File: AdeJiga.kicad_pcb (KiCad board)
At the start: 2 copper layers, 82 x 78 mm, 40 parts, among them J1 Screw_Terminal_01x03, J10 Conn_01x02_Pin, J11 Conn_01x02_Pin, J12 Screw_Terminal_01x03, J2 Screw_Terminal_01x02, J3 Screw_Terminal_01x03, J4 Conn_01x05_Pin, J5 Conn_01x02_Pin, J6 Conn_01x03_Pin, J7 Conn_01x02_Pin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

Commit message: Versão 3 consolidada, placa fabricada
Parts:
- added C3: 220uF, Capacitor_THT:CP_Radial_D6.3mm_P2.50mm, F.Cu at (174.0, 166.5)
- added D1: 1N4007, Diode_THT:D_DO-41_SOD81_P10.16mm_Horizontal, F.Cu at (137.5, 112.4)
- added D2: 1N4007, Diode_THT:D_DO-41_SOD81_P10.16mm_Horizontal, F.Cu at (137.5, 129.3)
- added D3: LED, LED_THT:LED_D5.0mm_Clear, F.Cu at (152.0, 115.2)
- added D4: 1N4007, Diode_THT:D_DO-41_SOD81_P10.16mm_Horizontal, F.Cu at (124.8, 166.2)
- added D5: LED, LED_THT:LED_D5.0mm_Clear, F.Cu at (152.1, 132.2)
- added D6: 1N4007, Diode_THT:D_DO-41_SOD81_P10.16mm_Horizontal, F.Cu at (137.5, 145.8)
- added D7: LED, LED_THT:LED_D5.0mm_Clear, F.Cu at (151.8, 151.8)
- added H1: MountingHole, MountingHole:MountingHole_3.2mm_M3_DIN965, F.Cu at (112.0, 175.2)
- added H2: MountingHole, MountingHole:MountingHole_3.2mm_M3_DIN965, F.Cu at (181.0, 175.7)
- added H3: MountingHole, MountingHole:MountingHole_3.2mm_M3_DIN965, F.Cu at (112.0, 104.7)
- added H4: MountingHole, MountingHole:MountingHole_3.2mm_M3_DIN965, F.Cu at (181.0, 104.7)
- added J1: Screw_Terminal_01x03, TerminalBlock_MetzConnect:TerminalBlock_MetzConnect_Type011_RT05503HBWC_1x03_P5.00mm_Horizontal, F.Cu at (115.3, 122.0)
- added J10: Conn_01x02_Pin, Connector_PinHeader_2.54mm:PinHeader_1x02_P2.54mm_Vertical, F.Cu at (171.8, 176.0)
- added J11: Conn_01x02_Pin, Connector_PinHeader_2.54mm:PinHeader_1x02_P2.54mm_Vertical, F.Cu at (118.5, 162.7)
- added J12: Screw_Terminal_01x03, TerminalBlock_MetzConnect:TerminalBlock_MetzConnect_Type011_RT05503HBWC_1x03_P5.00mm_Horizontal, F.Cu at (115.2, 156.0)
- added J2: Screw_Terminal_01x02, TerminalBlock_MetzConnect:TerminalBlock_MetzConnect_Type011_RT05502HBWC_1x02_P5.00mm_Horizontal, F.Cu at (118.8, 175.0)
- added J3: Screw_Terminal_01x03, TerminalBlock_MetzConnect:TerminalBlock_MetzConnect_Type011_RT05503HBWC_1x03_P5.00mm_Horizontal, F.Cu at (115.3, 139.0)
- added J4: Conn_01x05_Pin, Connector_PinSocket_2.54mm:PinSocket_1x05_P2.54mm_Vertical, F.Cu at (151.7, 103.0)
- added J5: Conn_01x02_Pin, Connector_PinHeader_2.54mm:PinHeader_1x02_P2.54mm_Vertical, F.Cu at (158.8, 130.7)
- added J6: Conn_01x03_Pin, Connector_PinHeader_2.54mm:PinHeader_1x03_P2.54mm_Vertical, F.Cu at (174.2, 124.7)
- added J7: Conn_01x02_Pin, Connector_PinHeader_2.54mm:PinHeader_1x02_P2.54mm_Vertical, F.Cu at (175.5, 176.0)
- added J8: Conn_01x03_Pin, Connector_PinHeader_2.54mm:PinHeader_1x03_P2.54mm_Vertical, F.Cu at (171.7, 103.0)
- added J9: Conn_01x04_Pin, Connector_PinHeader_2.54mm:PinHeader_1x04_P2.54mm_Vertical, F.Cu at (162.9, 103.0)
- added K1: JJM1C_relay, Benzlab:JJM1C_relay, F.Cu at (128.0, 117.0)
- added K2: JJM1C_relay, Benzlab:JJM1C_relay, F.Cu at (127.9, 134.0)
- added K3: JJM1C_relay, Benzlab:JJM1C_relay, F.Cu at (128.0, 149.7)
- added M1: DC-DC-STEP-DOWN-LM2596, Benzlab:DC-DC-STEP-DOWN-LM2596, F.Cu at (148.2, 168.2)
- added Q1: TIP127, Package_TO_SOT_THT:TO-220-3_Vertical, F.Cu at (145.3, 113.7)
- added Q2: TIP127, Package_TO_SOT_THT:TO-220-3_Vertical, F.Cu at (145.0, 147.5)
- added Q3: TIP127, Package_TO_SOT_THT:TO-220-3_Vertical, F.Cu at (145.1, 130.6)
- added R1: 3.3k, Resistor_THT:R_Axial_DIN0207_L6.3mm_D2.5mm_P10.16mm_Horizontal, F.Cu at (142.0, 122.2)
- added R2: 220, Resistor_THT:R_Axial_DIN0207_L6.3mm_D2.5mm_P10.16mm_Horizontal, F.Cu at (154.8, 123.2)
- added R3: 3.3k, Resistor_THT:R_Axial_DIN0207_L6.3mm_D2.5mm_P10.16mm_Horizontal, F.Cu at (141.8, 139.2)
- added R4: 220, Resistor_THT:R_Axial_DIN0207_L6.3mm_D2.5mm_P10.16mm_Horizontal, F.Cu at (155.1, 140.0)
- added R5: 0, Resistor_THT:R_Axial_DIN0204_L3.6mm_D1.6mm_P5.08mm_Vertical, F.Cu at (178.0, 121.7)
- added R7: 220, Resistor_THT:R_Axial_DIN0207_L6.3mm_D2.5mm_P10.16mm_Horizontal, F.Cu at (145.0, 157.0)
- added R8: 3.3k, Resistor_THT:R_Axial_DIN0207_L6.3mm_D2.5mm_P10.16mm_Horizontal, F.Cu at (141.8, 156.1)
- added U2: ESP32-WROOM-32, RF_Module:ESP32-WROOM-32, B.Cu at (169.3, 142.3)
- added U4: AMS1117, Package_TO_SOT_SMD:SOT-223-3_TabPin2, B.Cu at (174.2, 158.5)
- moved H1 77.1 mm to (112.0, 92.8), turned to -90 degrees
- moved H3 73.9 mm to (112.0, 22.2), turned to -90 degrees
- moved J2 70.3 mm to (118.8, 92.5), turned to 0 degrees
- moved H2 65.7 mm to (181.0, 93.2), turned to -90 degrees
- moved H4 64.3 mm to (181.0, 22.2), turned to -90 degrees
- moved J7 62.2 mm to (175.5, 93.5), turned to 180 degrees
- moved J10 59.6 mm to (171.8, 93.5), turned to 180 degrees
- moved J11 59.1 mm to (118.5, 80.2), turned to 90 degrees
- moved J12 58.2 mm to (115.2, 73.5), turned to 90 degrees
- moved J8 57.6 mm to (171.7, 20.5), turned to -90 degrees
- moved J1 57.5 mm to (115.3, 39.5), turned to 90 degrees
- moved D4 55.4 mm to (124.8, 83.8), turned to 180 degrees
- moved J9 52.8 mm to (162.9, 20.5), turned to -90 degrees
- moved J3 52.5 mm to (115.3, 56.5), turned to 90 degrees
- moved J4 50.7 mm to (151.7, 20.5), turned to -90 degrees
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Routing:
- net GND: track 283.2 -> 554.3 mm
- net +5V: track 202.5 -> 416.6 mm
- net GPIOA: track 37.7 -> 74.2 mm
- net GPIOB: track 37.1 -> 73.1 mm
- net GPIOC: track 36.9 -> 72.1 mm
- net GPIOD: track 35.6 -> 70.1 mm
- net GPIOE: track 35.1 -> 69.1 mm
- net GPIOF: track 34.6 -> 68.0 mm
- net GPIOG: track 34.1 -> 67.3 mm
- net GPIOH: track 33.0 -> 65.0 mm
- net REL3: track 29.2 -> 58.4 mm
- net +3.3V: track 25.0 -> 50.0 mm
- net REL2: track 23.2 -> 46.3 mm
- net REL1: track 25.6 -> 47.4 mm
- net Net-(J12-Pin_2): track 20.2 -> 40.5 mm
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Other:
- board size 82 x 78 mm -> 78 x 162.2 mm
- board text removed: "-"
- board text removed: "3V3"
- board text removed: "5V"
- board text removed: "A"
- board text removed: "B"
- board text removed: "C"
- board text removed: "D"
- board text removed: "E"
- board text removed: "F"
- board text removed: "G"
- board text removed: "H"
- board text removed: "NA"
- board text removed: "NF"

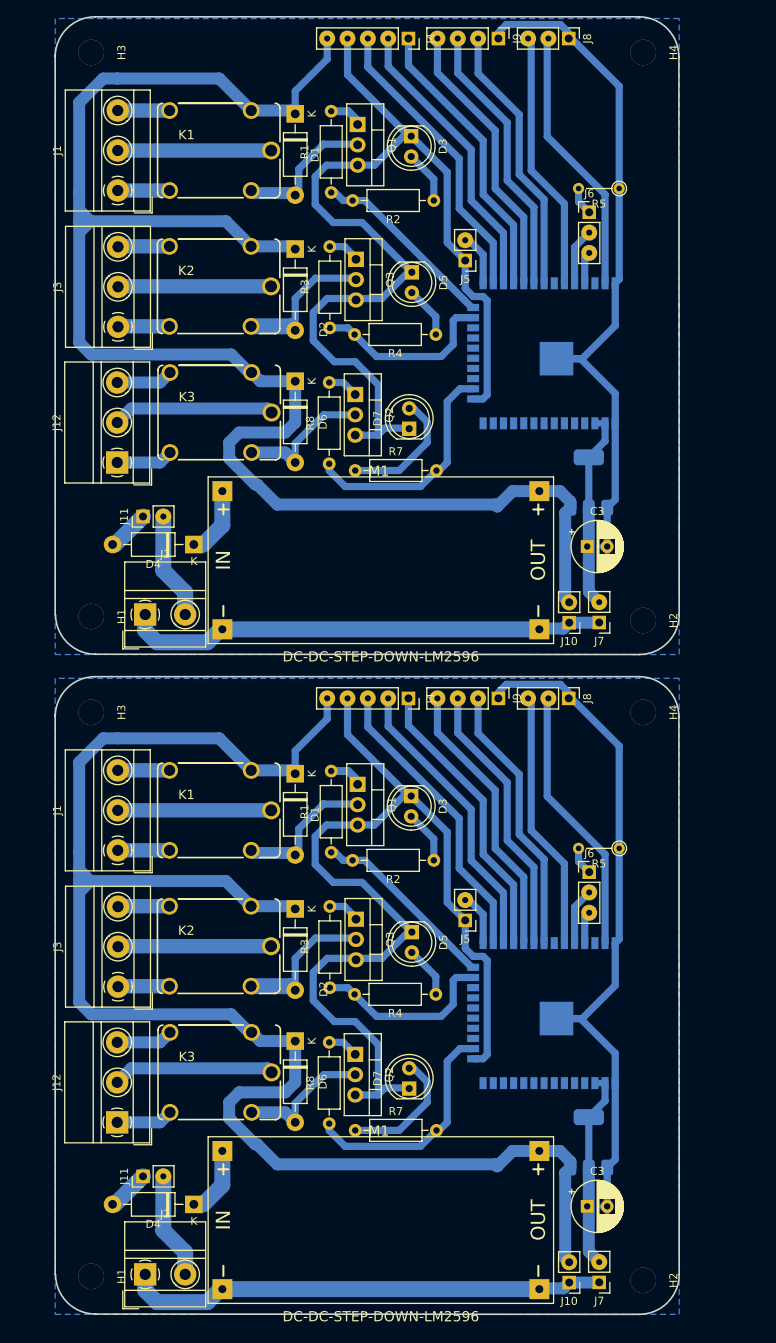
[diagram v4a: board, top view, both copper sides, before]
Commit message: modificações no layout da placa e modelo 3d
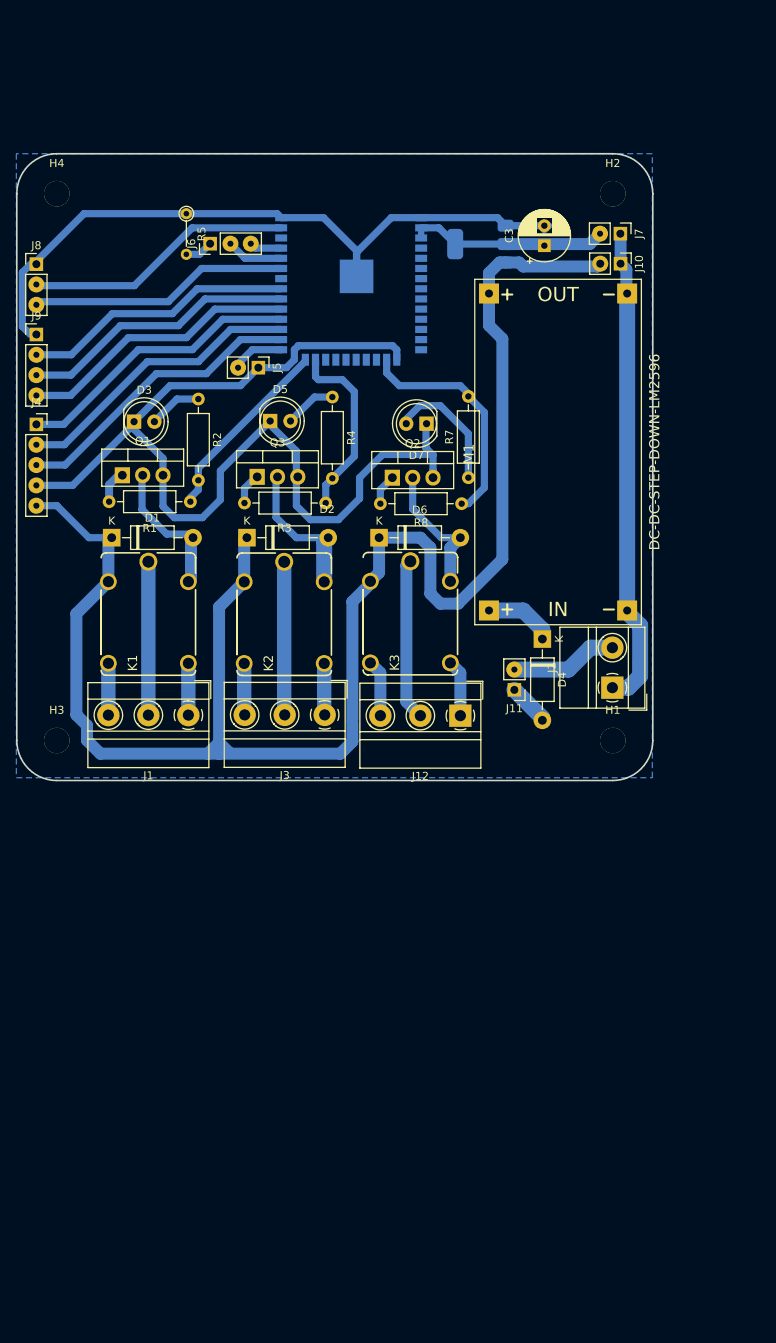
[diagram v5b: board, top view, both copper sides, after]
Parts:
- removed the C3 at (174.0, 166.5)
- removed the D1 at (137.5, 112.4)
- removed the D2 at (137.5, 129.3)
- removed the D3 at (152.0, 115.2)
- removed the D4 at (124.8, 166.2)
- removed the D5 at (152.1, 132.2)
- removed the D6 at (137.5, 145.8)
- removed the D7 at (151.8, 151.8)
- removed the H1 at (112.0, 175.2)
- removed the H2 at (181.0, 175.7)
- removed the H3 at (112.0, 104.7)
- removed the H4 at (181.0, 104.7)
- removed the J1 at (115.3, 122.0)
- removed the J10 at (171.8, 176.0)
- removed the J11 at (118.5, 162.7)
- removed the J12 at (115.2, 156.0)
- removed the J2 at (118.8, 175.0)
- removed the J3 at (115.3, 139.0)
- removed the J4 at (151.7, 103.0)
- removed the J5 at (158.8, 130.7)
- removed the J6 at (174.2, 124.7)
- removed the J7 at (175.5, 176.0)
- removed the J8 at (171.7, 103.0)
- removed the J9 at (162.9, 103.0)
- removed the K1 at (128.0, 117.0)
- removed the K2 at (127.9, 134.0)
- removed the K3 at (128.0, 149.7)
- removed the M1 at (148.2, 168.2)
- removed the Q1 at (145.3, 113.7)
- removed the Q2 at (145.0, 147.5)
- removed the Q3 at (145.1, 130.6)
- removed the R1 at (142.0, 122.2)
- removed the R2 at (154.8, 123.2)
- removed the R3 at (141.8, 139.2)
- removed the R4 at (155.1, 140.0)
- removed the R5 at (178.0, 121.7)
- removed the R7 at (145.0, 157.0)
- removed the R8 at (141.8, 156.1)
- removed the U2 at (169.3, 142.3)
- removed the U4 at (174.2, 158.5)
- moved H3 86.1 mm to (107.7, 108.2), turned to 0 degrees
- moved H4 75.4 mm to (107.7, 39.9), turned to 0 degrees
- moved J8 72.3 mm to (105.1, 48.7), turned to 0 degrees
- moved J9 68.6 mm to (105.1, 57.5), turned to 0 degrees
- moved H1 67.0 mm to (177.2, 108.2), turned to 0 degrees
- moved J4 67.0 mm to (105.1, 68.7), turned to 0 degrees
- moved J1 66.2 mm to (124.1, 105.1), turned to 180 degrees
- moved J2 59.1 mm to (177.1, 101.6), turned to 90 degrees
- moved K1 58.6 mm to (119.1, 92.4), turned to 90 degrees
- moved D1 57.7 mm to (114.6, 82.9), turned to 0 degrees
- moved J3 55.0 mm to (141.2, 105.0), turned to 180 degrees
- moved R5 54.2 mm to (123.9, 42.4), turned to -90 degrees
- moved H2 53.5 mm to (177.2, 39.9), turned to 0 degrees
- moved J12 53.3 mm to (158.1, 105.1), turned to 180 degrees
- moved Q1 52.8 mm to (115.9, 75.1), turned to 0 degrees
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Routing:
- net GND: track 554.3 -> 277.1 mm
- net +5V: track 416.6 -> 208.1 mm
- net GPIOA: track 74.2 -> 37.1 mm
- net GPIOB: track 73.1 -> 36.6 mm
- net GPIOC: track 72.1 -> 36.0 mm
- net GPIOD: track 70.1 -> 35.1 mm
- net GPIOE: track 69.1 -> 34.5 mm
- net GPIOF: track 68.0 -> 34.0 mm
- net GPIOG: track 67.3 -> 33.7 mm
- net GPIOH: track 65.0 -> 32.5 mm
- net REL3: track 58.4 -> 29.2 mm
- net +3.3V: track 50.0 -> 25.0 mm
- net REL1: track 47.4 -> 23.7 mm
- net REL2: track 46.3 -> 23.2 mm
- net Net-(J12-Pin_2): track 40.5 -> 20.2 mm
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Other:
- board size 78 x 162.2 mm -> 79.5 x 78.3 mm
